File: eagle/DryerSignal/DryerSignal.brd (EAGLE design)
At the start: 32 x 60 mm, 18 parts, among them J1 4.5v, P1 INPUT, T1 2N3904, U1 MCP1755T-3302E/OT, U2 ATTINY85

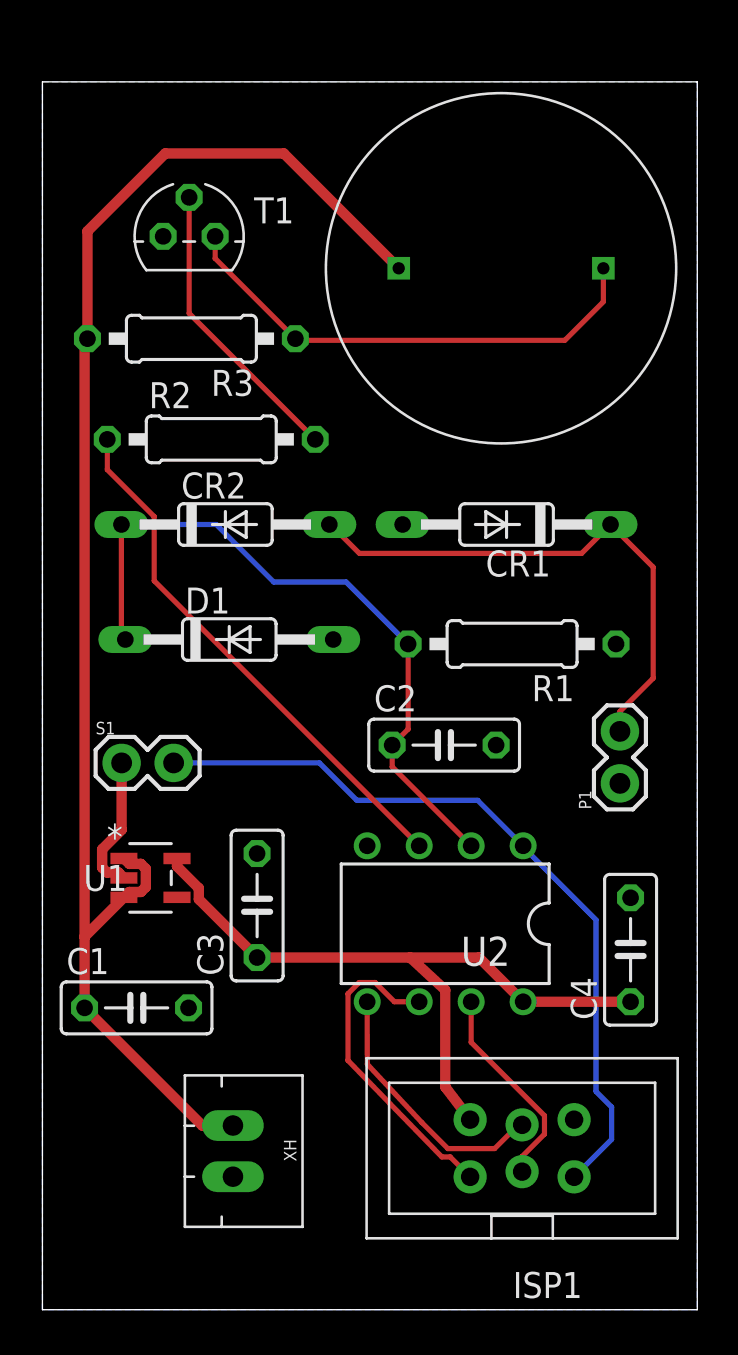
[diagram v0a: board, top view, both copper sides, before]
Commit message: updated schematic & board to remove voltage regulator
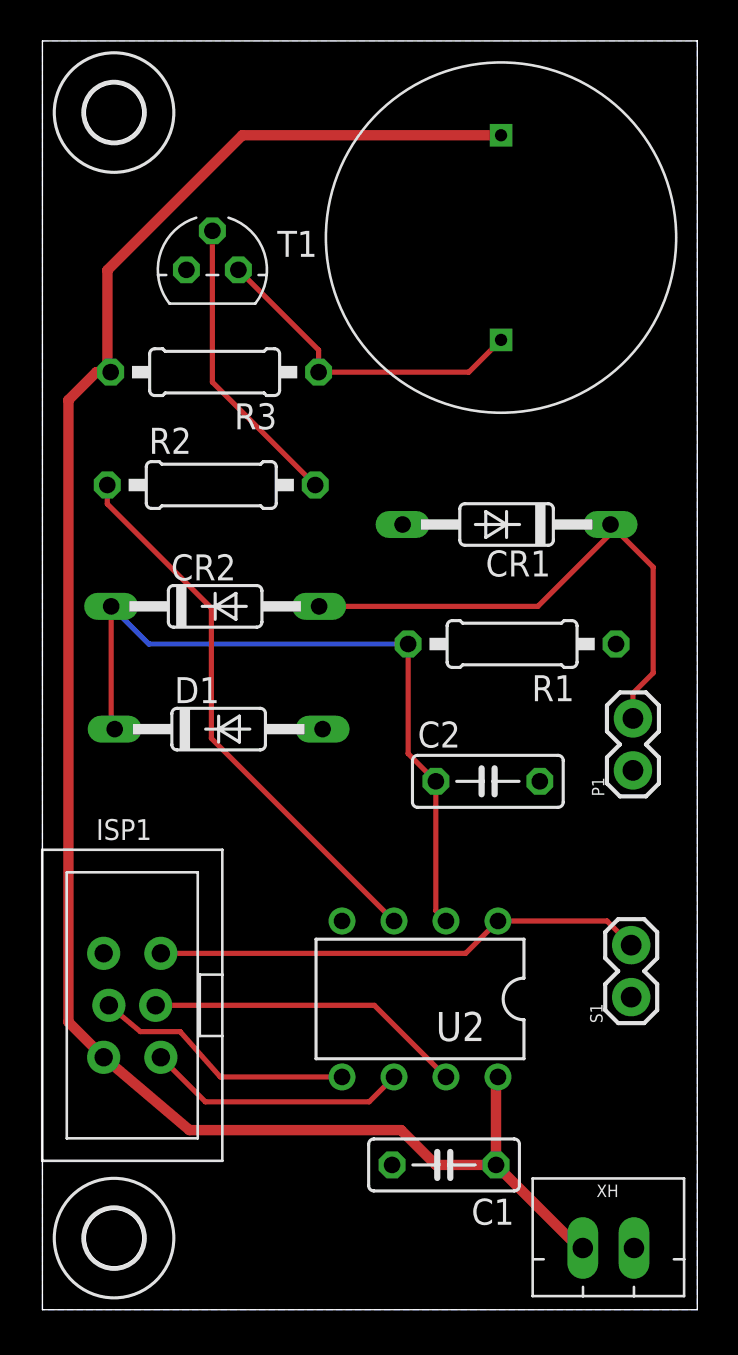
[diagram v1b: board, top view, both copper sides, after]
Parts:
- removed C3, C4: 1uf, DryerSignal:C050-025X075
- removed U1: MCP1755T-3302E/OT, DryerSignal:SOT-23-5_MC
- added H1, H2: MOUNT-HOLE2.8, DryerSignal:2,8
- moved S1 27.4 mm to (28.8, 15.3), turned to 90 degrees
- moved ISP1 20.3 mm to (4.39, 14.9), turned to 180 degrees
- moved J1 18.8 mm to (31.4, 6.42), turned to 180 degrees
- moved C1 16.9 mm to (19.6, 7.08), turned to 180 degrees
- moved D1 4.41 mm to (8.61, 28.4)
- moved CR2 4.03 mm to (8.44, 34.4)
- moved U2 3.88 mm to (18.4, 15.2)
- moved C2 2.77 mm to (21.8, 25.8)
- moved R2 2.23 mm to (8.25, 40.3)
- moved T1 1.99 mm to (8.30, 50.8)
- moved R3 1.99 mm to (8.41, 45.8)
- moved SG1 1.50 mm to (22.4, 52.4), turned to 270 degrees
- moved P1 0.90 mm to (28.9, 26.4)
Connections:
- removed net VIN: C1.1, J1.2, R3.2, SG1.P$1, U1.1, U1.3
- net GND: no longer C3.2, C4.2, U1.2
- net VCC: now also C1.1, J1.2, R3.2, SG1.P$1; no longer C3.1, C4.1, U1.5
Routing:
- net VIN: track 72.9 -> 0.00 mm
- net VCC: track 34.7 -> 93.9 mm
- net RST: track 37.5 -> 24.1 mm
- net N$2: track 24.1 -> 16.2 mm
- net GND: track 6.79 -> 0.00 mm
- net SCK: track 10.2 -> 15.6 mm
- net MISO: track 15.7 -> 12.8 mm
- net ANLG: track 33.9 -> 35.6 mm
- net TONE: track 26.2 -> 27.1 mm
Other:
- board size 32 x 60 mm -> 32 x 62 mm
- board text added: "DryerSignal 1.0"
